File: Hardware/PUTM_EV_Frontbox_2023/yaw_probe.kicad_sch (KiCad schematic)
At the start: 9 parts, among them IC1 ELVH-MF12D-HRRJ-C-N3A4, IC2 ELVH-MF12D-HRRJ-C-N3A4

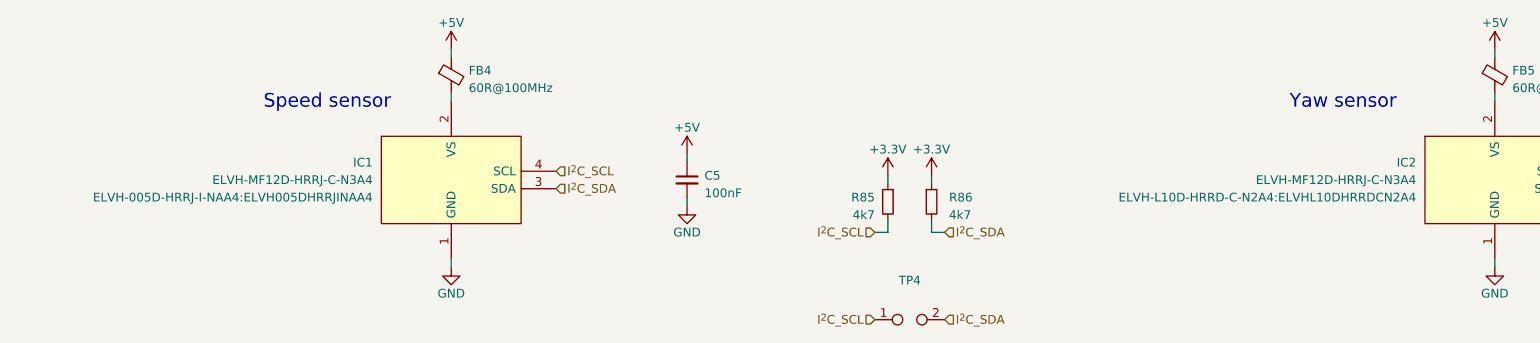
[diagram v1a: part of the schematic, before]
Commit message: Schematic modified, footprints assigned
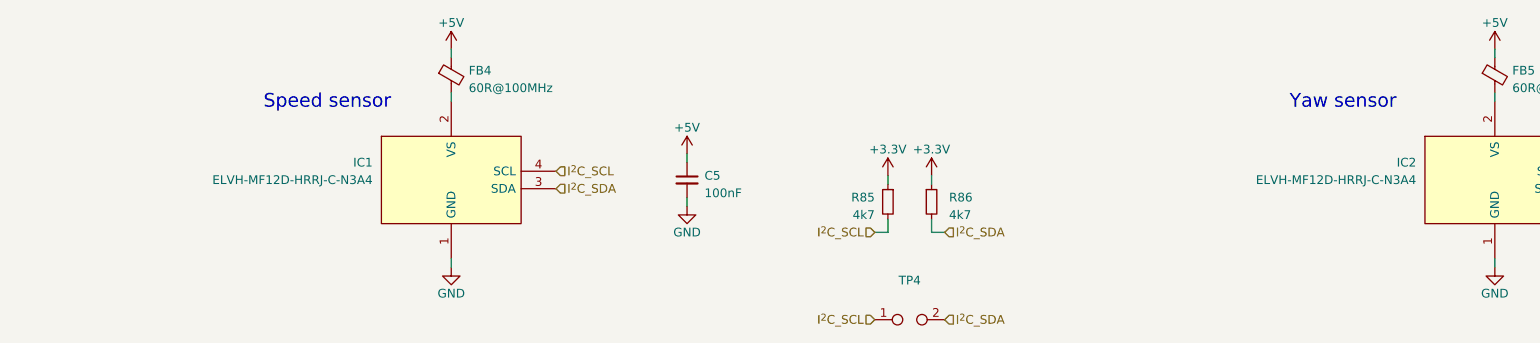
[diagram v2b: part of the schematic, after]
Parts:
- C40, C5: footprint (none) -> Capacitor_SMD:C_0402_1005Metric_Pad0.74x0.62mm_HandSolder
- FB4, FB5: footprint (none) -> Inductor_SMD:L_0603_1608Metric
- IC1: footprint ELVH-005D-HRRJ-I-NAA4:ELVH005DHRRJINAA4 -> Frontbox:ELVH005DHRRJINAA4
- IC2: footprint ELVH-L10D-HRRD-C-N2A4:ELVHL10DHRRDCN2A4 -> Frontbox:ELVHL10DHRRDCN2A4
- R85, R86: footprint (none) -> Resistor_SMD:R_0402_1005Metric
- TP4: footprint (none) -> TestPoint:TestPoint_2Pads_Pitch2.54mm_Drill0.8mm
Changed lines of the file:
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@@
       (effects (font (size 1.27 1.27)) (justify left))
     )
-    (property "Footprint" "" (at 139.065 99.06 0)
+    (property "Footprint" "Resistor_SMD:R_0402_1005Metric" (at 139.065 99.06 0)
       (effects (font (size 1.27 1.27)) hide)
     )
@@
       (effects (font (size 1.27 1.27)) (justify left))
     )
-    (property "Footprint" "" (at 109.855 95.885 0)
+    (property "Footprint" "Capacitor_SMD:C_0402_1005Metric_Pad0.74x0.62mm_HandSolder" (at 109.855 95.885 0)
       (effects (font (size 1.27 1.27)) hide)
     )
@@
       (effects (font (size 1.27 1.27)) (justify left))
     )
-    (property "Footprint" "" (at 225.552 80.645 90)
+    (property "Footprint" "Inductor_SMD:L_0603_1608Metric" (at 225.552 80.645 90)
       (effects (font (size 1.27 1.27)) hide)
     )
@@
       (effects (font (size 1.27 1.27)) (justify left))
     )
-    (property "Footprint" "" (at 73.787 80.645 90)
+    (property "Footprint" "Inductor_SMD:L_0603_1608Metric" (at 73.787 80.645 90)
       (effects (font (size 1.27 1.27)) hide)
     )
@@
       (effects (font (size 1.27 1.27)) (justify left))
     )
-    (property "Footprint" "" (at 145.415 99.06 0)
+    (property "Footprint" "Resistor_SMD:R_0402_1005Metric" (at 145.415 99.06 0)
       (effects (font (size 1.27 1.27)) hide)
     )
@@
       (effects (font (size 1.27 1.27)) (justify right))
     )
-    (property "Footprint" "ELVH-L10D-HRRD-C-N2A4:ELVHL10DHRRDCN2A4" (at 215.9 98.4249 0)
-      (effects (font (size 1.27 1.27)) (justify right))
+    (property "Footprint" "Frontbox:ELVHL10DHRRDCN2A4" (at 215.9 98.4249 0)
+      (effects (font (size 1.27 1.27)) (justify right) hide)
     )
     (property "Datasheet" "https://www.allsensors.com/datasheets/DS-0376_Rev_A.pdf" (at 173.99 108.585 0)
@@
       (effects (font (size 1.27 1.27)) hide)
     )
-    (property "Footprint" "" (at 142.24 116.205 0)
+    (property "Footprint" "TestPoint:TestPoint_2Pads_Pitch2.54mm_Drill0.8mm" (at 142.24 116.205 0)
       (effects (font (size 1.27 1.27)) hide)
     )
@@
       (effects (font (size 1.27 1.27)) (justify left))
     )
-    (property "Footprint" "" (at 265.43 95.885 0)
+    (property "Footprint" "Capacitor_SMD:C_0402_1005Metric_Pad0.74x0.62mm_HandSolder" (at 265.43 95.885 0)
       (effects (font (size 1.27 1.27)) hide)
     )
@@
       (effects (font (size 1.27 1.27)) (justify right))
     )
-    (property "Footprint" "ELVH-005D-HRRJ-I-NAA4:ELVH005DHRRJINAA4" (at 64.135 98.4249 0)
-      (effects (font (size 1.27 1.27)) (justify right))
+    (property "Footprint" "Frontbox:ELVH005DHRRJINAA4" (at 64.135 98.4249 0)
+      (effects (font (size 1.27 1.27)) (justify right) hide)
     )
     (property "Datasheet" "https://www.allsensors.com/datasheets/DS-0376_Rev_A.pdf" (at 22.225 108.585 0)

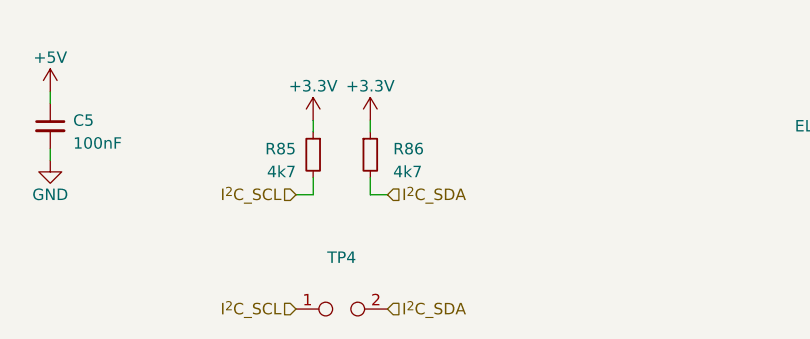
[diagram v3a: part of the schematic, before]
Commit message: Redid component placement
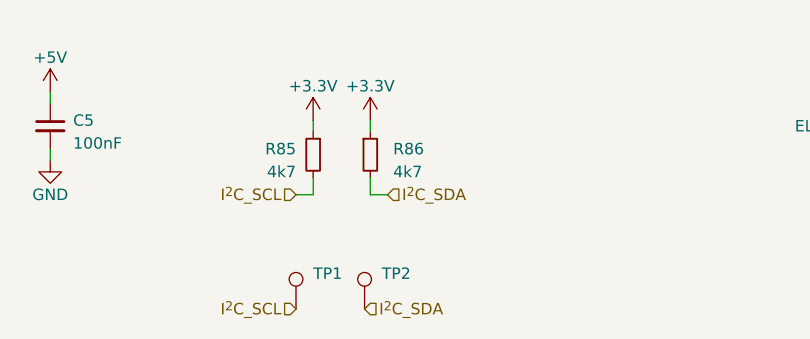
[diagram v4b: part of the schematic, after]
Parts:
- removed TP4: TestPoint_2Pole, TestPoint:TestPoint_2Pads_Pitch2.54mm_Drill0.8mm, symbol Connector:TestPoint_2Pole
- added TP1, TP2: TestPoint, TestPoint:TestPoint_Pad_1.0x1.0mm, symbol Connector:TestPoint
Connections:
- net I^{2}C_SCL: now also TP1.1
- net I^{2}C_SDA: now also TP2.1
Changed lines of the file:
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@@
     (effects (font (size 2 2)) (justify left bottom))
   )
-  (hierarchical_label "I^{2}C_SDA" (shape input) (at 147.32 116.205 0) (fields_autoplaced)
+  (hierarchical_label "I^{2}C_SDA" (shape input) (at 144.78 116.205 0) (fields_autoplaced)
     (effects (font (size 1.27 1.27)) (justify left))
   )
@@
     )
   )
-  (symbol (lib_id "Connector:TestPoint_2Pole") (at 142.24 116.205 0) (unit 1)
-    (in_bom yes) (on_board yes) (dnp no)
-    (property "Reference" "TP4" (at 142.24 110.49 0)
-      (effects (font (size 1.27 1.27)))
-    )
-    (property "Value" "TestPoint_2Pole" (at 142.24 113.03 0)
-      (effects (font (size 1.27 1.27)) hide)
-    )
-    (property "Footprint" "TestPoint:TestPoint_2Pads_Pitch2.54mm_Drill0.8mm" (at 142.24 116.205 0)
-      (effects (font (size 1.27 1.27)) hide)
-    )
-    (property "Datasheet" "~" (at 142.24 116.205 0)
-      (effects (font (size 1.27 1.27)) hide)
-    )
-    (pin "1")
-    (pin "2")
-    (instances
-      (project "PUTM_EV_Frontbox_2023"
-        (path "/b652b05a-4e3d-4ad1-b032-18886abe7d45/ba538a3c-1084-4770-aed2-08b4305d2379"
-          (reference "TP4") (unit 1)
-        )
-      )
-    )
-  )
   (symbol (lib_id "Device:C_Small") (at 265.43 95.885 0) (unit 1)
     (in_bom yes) (on_board yes) (dnp no) (fields_autoplaced)
@@
         (path "/b652b05a-4e3d-4ad1-b032-18886abe7d45/ba538a3c-1084-4770-aed2-08b4305d2379"
           (reference "C40") (unit 1)
+        )
+      )
+    )
+  )
+  (symbol (lib_id "Connector:TestPoint") (at 144.78 116.205 0) (unit 1)
+    (in_bom yes) (on_board yes) (dnp no) (fields_autoplaced)
+    (property "Reference" "TP2" (at 146.685 112.268 0)
+      (effects (font (size 1.27 1.27)) (justify left))
+    )
+    (property "Value" "TestPoint" (at 146.685 114.808 0)
+      (effects (font (size 1.27 1.27)) (justify left) hide)
+    )
+    (property "Footprint" "TestPoint:TestPoint_Pad_1.0x1.0mm" (at 149.86 116.205 0)
+      (effects (font (size 1.27 1.27)) hide)
+    )
+    (property "Datasheet" "~" (at 149.86 116.205 0)
+      (effects (font (size 1.27 1.27)) hide)
+    )
+    (pin "1")
+    (instances
+      (project "PUTM_EV_Frontbox_2023"
+        (path "/b652b05a-4e3d-4ad1-b032-18886abe7d45/79afe43e-babf-4d5d-a636-ae8293b09b20"
+          (reference "TP2") (unit 1)
+        )
+        (path "/b652b05a-4e3d-4ad1-b032-18886abe7d45/ba538a3c-1084-4770-aed2-08b4305d2379"
+          (reference "TP5") (unit 1)
         )
       )
@@
         )
       )
+    )
+  )
+  (symbol (lib_id "Connector:TestPoint") (at 137.16 116.205 0) (unit 1)
+    (in_bom yes) (on_board yes) (dnp no) (fields_autoplaced)
+    (property "Reference" "TP1" (at 139.065 112.268 0)
+      (effects (font (size 1.27 1.27)) (justify left))
+    )
+    (property "Value" "TestPoint" (at 139.065 114.808 0)
+      (effects (font (size 1.27 1.27)) (justify left) hide)
+    )
+    (property "Footprint" "TestPoint:TestPoint_Pad_1.0x1.0mm" (at 142.24 116.205 0)
+      (effects (font (size 1.27 1.27)) hide)
+    )
+    (property "Datasheet" "~" (at 142.24 116.205 0)
+      (effects (font (size 1.27 1.27)) hide)
+    )
+    (pin "1")
+    (instances
+      (project "PUTM_EV_Frontbox_2023"
+        (path "/b652b05a-4e3d-4ad1-b032-18886abe7d45/79afe43e-babf-4d5d-a636-ae8293b09b20"
+          (reference "TP1") (unit 1)
+        )
+        (path "/b652b05a-4e3d-4ad1-b032-18886abe7d45/ba538a3c-1084-4770-aed2-08b4305d2379"
+          (reference "TP4") (unit 1)
+        )
+      )

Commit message: Ready for production
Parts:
- added J4: USB_C_Receptacle, Frontbox:CUI_UJ31-CH-31-SMT-TR, symbol Connector:USB_C_Receptacle
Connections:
- new net: J4.A1 (GND), J4.A12 (GND), J4.B1 (GND), J4.B12 (GND)
- new net: J4.A4 (VBUS), J4.A9 (VBUS), J4.B4 (VBUS), J4.B9 (VBUS)
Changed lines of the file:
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@@
+    )
+  )
+  (symbol (lib_id "Connector:USB_C_Receptacle") (at 105.41 141.605 0) (unit 1)
+    (in_bom yes) (on_board yes) (dnp no) (fields_autoplaced)
+    (property "Reference" "J4" (at 105.41 109.855 0)
+      (effects (font (size 1.27 1.27)))
+    )
+    (property "Value" "USB_C_Receptacle" (at 105.41 112.395 0)
+      (effects (font (size 1.27 1.27)))
+    )
+    (property "Footprint" "Frontbox:CUI_UJ31-CH-31-SMT-TR" (at 109.22 141.605 0)
+      (effects (font (size 1.27 1.27)) hide)
+    )
+    (property "Datasheet" "https://eu.mouser.com/ProductDetail/GCT/USB4085-GF-A?qs=KUoIvG%2F9Ilba1bQOahfWjw%3D%3D" (at 109.22 141.605 0)
+      (effects (font (size 1.27 1.27)) hide)
+    )
+    (pin "A1")
+    (pin "A10")
+    (pin "A11")
+    (pin "A12")
+    (pin "A2")
+    (pin "A3")
+    (pin "A4")
+    (pin "A5")
+    (pin "A6")
+    (pin "A7")
+    (pin "A8")
+    (pin "A9")
+    (pin "B1")
+    (pin "B10")
+    (pin "B11")
+    (pin "B12")
+    (pin "B2")
+    (pin "B3")
+    (pin "B4")
+    (pin "B5")
+    (pin "B6")
+    (pin "B7")
+    (pin "B8")
+    (pin "B9")
+    (pin "S1")
+    (instances
+      (project "PUTM_EV_Frontbox_2023"
+        (path "/b652b05a-4e3d-4ad1-b032-18886abe7d45"
+          (reference "J4") (unit 1)
+        )
+        (path "/b652b05a-4e3d-4ad1-b032-18886abe7d45/ba538a3c-1084-4770-aed2-08b4305d2379"
+          (reference "J4") (unit 1)
+        )
+      )
     )
   )

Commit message: PCB taken apart
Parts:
- removed J4: USB_C_Receptacle, Frontbox:CUI_UJ31-CH-31-SMT-TR, symbol Connector:USB_C_Receptacle
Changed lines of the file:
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@@
-    )
-  )
-  (symbol (lib_id "Connector:USB_C_Receptacle") (at 105.41 141.605 0) (unit 1)
-    (in_bom yes) (on_board yes) (dnp no) (fields_autoplaced)
-    (property "Reference" "J4" (at 105.41 109.855 0)
-      (effects (font (size 1.27 1.27)))
-    )
-    (property "Value" "USB_C_Receptacle" (at 105.41 112.395 0)
-      (effects (font (size 1.27 1.27)))
-    )
-    (property "Footprint" "Frontbox:CUI_UJ31-CH-31-SMT-TR" (at 109.22 141.605 0)
-      (effects (font (size 1.27 1.27)) hide)
-    )
-    (property "Datasheet" "https://eu.mouser.com/ProductDetail/GCT/USB4085-GF-A?qs=KUoIvG%2F9Ilba1bQOahfWjw%3D%3D" (at 109.22 141.605 0)
-      (effects (font (size 1.27 1.27)) hide)
-    )
-    (pin "A1")
-    (pin "A10")
-    (pin "A11")
-    (pin "A12")
-    (pin "A2")
-    (pin "A3")
-    (pin "A4")
-    (pin "A5")
-    (pin "A6")
-    (pin "A7")
-    (pin "A8")
-    (pin "A9")
-    (pin "B1")
-    (pin "B10")
-    (pin "B11")
-    (pin "B12")
-    (pin "B2")
-    (pin "B3")
-    (pin "B4")
-    (pin "B5")
-    (pin "B6")
-    (pin "B7")
-    (pin "B8")
-    (pin "B9")
-    (pin "S1")
-    (instances
-      (project "PUTM_EV_Frontbox_2023"
-        (path "/b652b05a-4e3d-4ad1-b032-18886abe7d45"
-          (reference "J4") (unit 1)
-        )
-        (path "/b652b05a-4e3d-4ad1-b032-18886abe7d45/ba538a3c-1084-4770-aed2-08b4305d2379"
-          (reference "J4") (unit 1)
-        )
-      )
     )
   )

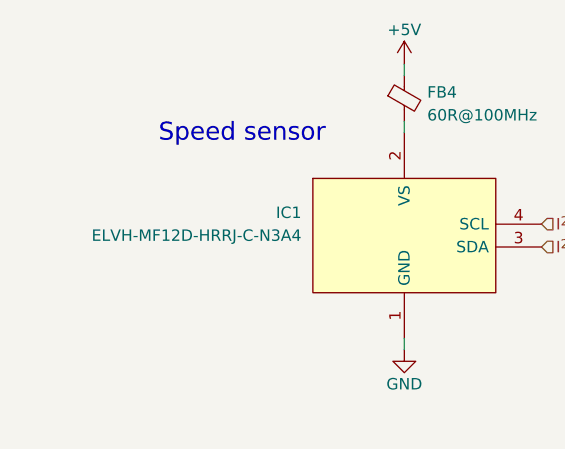
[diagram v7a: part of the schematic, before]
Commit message: Changed mcu pinout
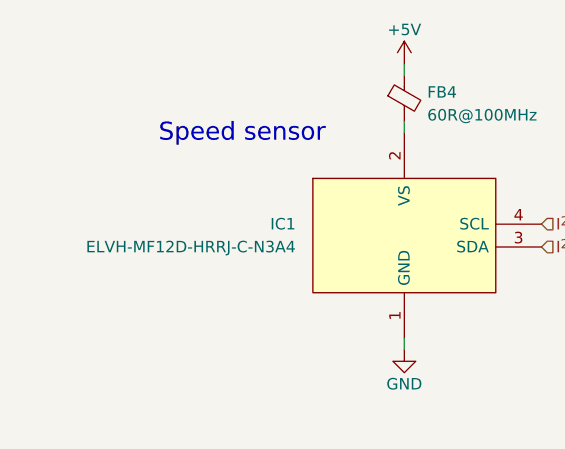
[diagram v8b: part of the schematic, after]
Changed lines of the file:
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@@
   (symbol (lib_id "YAW_PROBE:ELVH-MF12D-HRRJ-C-N3A4") (at 60.325 92.075 0) (unit 1)
     (in_bom yes) (on_board yes) (dnp no) (fields_autoplaced)
-    (property "Reference" "IC1" (at 64.135 93.3449 0)
+    (property "Reference" "IC1" (at 63.5 94.615 0)
       (effects (font (size 1.27 1.27)) (justify right))
     )
-    (property "Value" "ELVH-MF12D-HRRJ-C-N3A4" (at 64.135 95.8849 0)
+    (property "Value" "ELVH-MF12D-HRRJ-C-N3A4" (at 63.5 97.155 0)
       (effects (font (size 1.27 1.27)) (justify right))
     )
